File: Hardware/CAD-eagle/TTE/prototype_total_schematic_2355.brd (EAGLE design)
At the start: 39.5 x 44.9 mm, 31 parts, among them J2 MOLEX_48037-0001MOLEX_48037-0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, J4 RX

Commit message: Cascaded RX PGA array confirmed
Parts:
- added C7: 22pF, SparkFun-Capacitors:0805
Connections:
- new net ANTENNA_TX_SIG_COUPLED: C7.2, TM2.3
- net ANTENNA_TX_SIG: now also C7.1; no longer TM2.3
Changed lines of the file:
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@@
 <attribute name="PROD_ID" value="CONN-09696" x="23.114" y="24.384" size="1.778" layer="27" display="off"/>
+</element>
+<element name="C7" library="SparkFun-Capacitors" package="0805" value="22pF" x="11.43" y="-16.764">
+<attribute name="PROD_ID" value="CAP-08402" x="11.43" y="-16.764" size="1.778" layer="27" display="off"/>
 </element>
 </elements>
@@
 <signal name="ANTENNA_TX_SIG">
 <contactref element="MSP430" pad="34"/>
-<contactref element="TM2" pad="3"/>
 <contactref element="SIG" pad="2"/>
 <wire x1="25.7556" y1="35.9664" x2="21.1836" y2="31.3944" width="0.508" layer="1"/>
@@
 <wire x1="32.004" y1="39.624" x2="30.3276" y2="39.624" width="0.1524" layer="16"/>
 <wire x1="33.274" y1="38.354" x2="32.004" y2="39.624" width="0.1524" layer="16"/>
-<wire x1="21.1836" y1="31.3944" x2="21.035" y2="31.258" width="0.1524" layer="1"/>
 <wire x1="42.3672" y1="30.0228" x2="43.2816" y2="30.0228" width="0.1524" layer="1"/>
 <wire x1="41.148" y1="31.242" x2="42.3672" y2="30.0228" width="0.1524" layer="1"/>
@@
 <via x="25.7556" y="35.9664" extent="1-16" drill="0.35"/>
 <via x="41.148" y="31.242" extent="1-16" drill="0.35"/>
+<contactref element="C7" pad="1"/>
+<wire x1="10.53" y1="-16.764" x2="21.1836" y2="31.3944" width="0" layer="19" extent="1-1"/>
 </signal>
 <signal name="RX_PGA_1">
@@
 <via x="41.6052" y="10.0584" extent="1-16" drill="0.35"/>
 </signal>
+<signal name="ANTENNA_TX_SIG_COUPLED">
+<contactref element="TM2" pad="3"/>
+<contactref element="C7" pad="2"/>
+<wire x1="12.33" y1="-16.764" x2="21.035" y2="31.258" width="0" layer="19" extent="1-1"/>
+</signal>
 </signals>

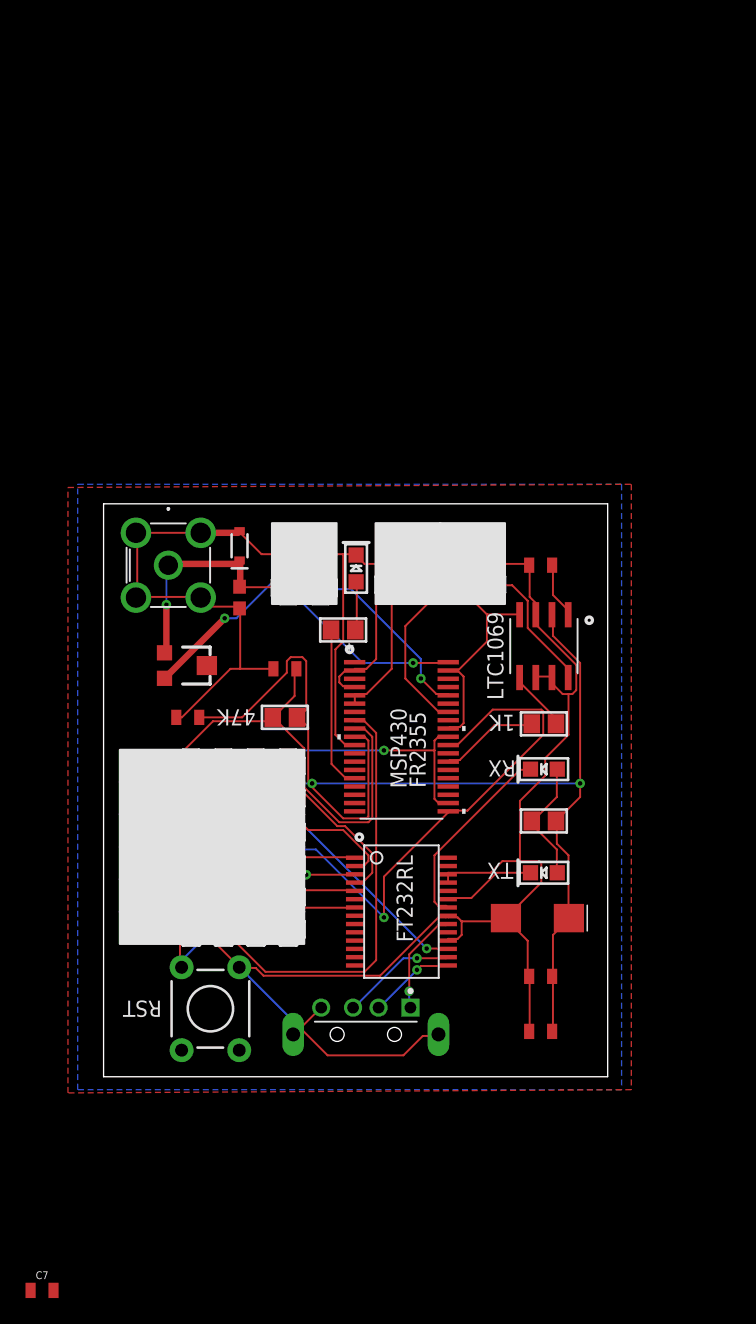
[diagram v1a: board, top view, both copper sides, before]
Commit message: Reciever Pipeline Confirmed, Updated Gerbers, included tx coupling capacitor for rx offset
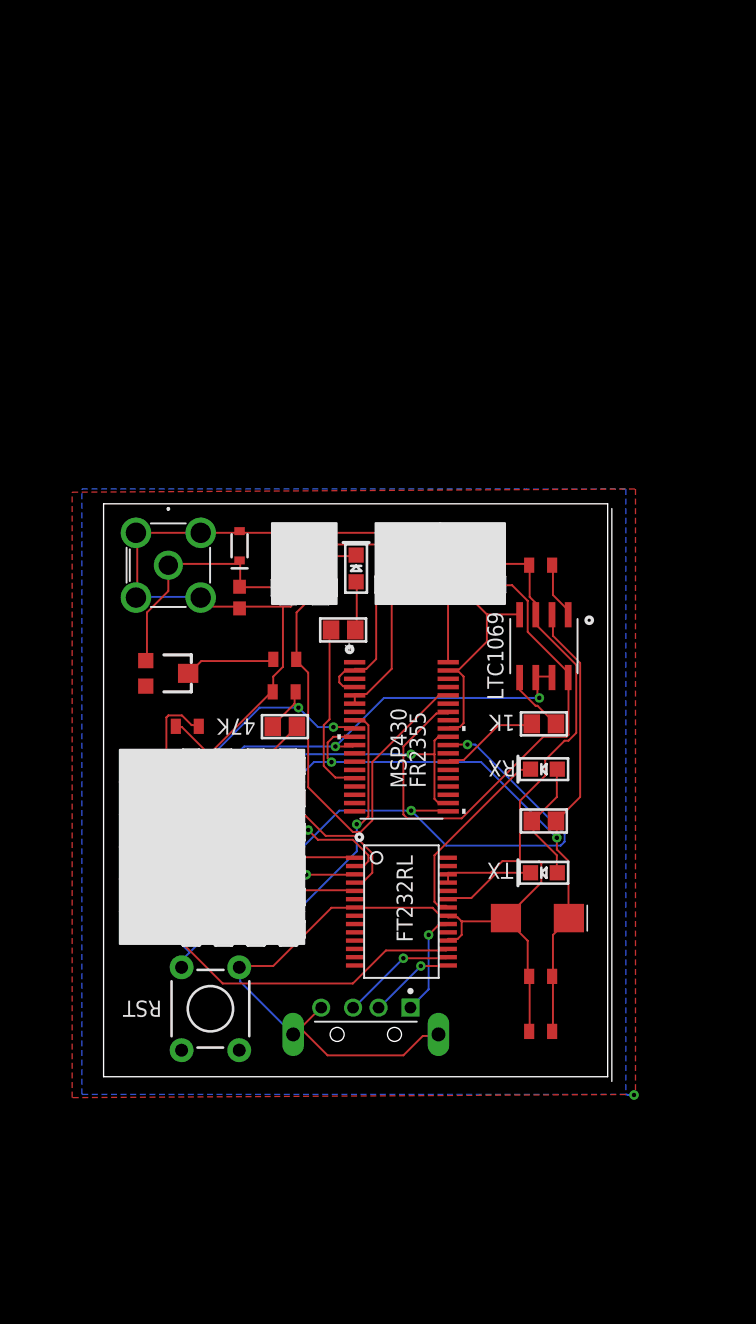
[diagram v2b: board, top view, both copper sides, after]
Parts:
- C5: value 100n -> .1u
- C7: value 22pF -> 22p
- moved C7 53.0 mm to (30.5, 32.7), turned to 180 degrees
- moved C6 1.81 mm to (30.4, 30.2)
- moved TM2 1.59 mm to (21.4, 31.6)
- moved 47K 0.73 mm to (30.5, 27.5)
- moved C5 0.70 mm to (22.8, 27.5)
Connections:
- removed net ANTENNA_TX_SIG_COUPLED: C7.2, TM2.3
- new net N$2: C7.2, TM2.2
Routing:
- net RST/SBWTDIO: track 58.7 -> 41.8 mm, vias 0 -> 2
- net FILTER_OUT: track 29.0 -> 41.3 mm
- net VCC_USB: track 45.3 -> 54.3 mm, vias 1 -> 0
- net TEST/SSBWTCK: track 33.7 -> 24.7 mm, vias 0 -> 1
- net VCC: track 98.4 -> 90.7 mm
- net ANTENNA_SIG: track 34.0 -> 41.4 mm, vias 2 -> 0
- net N$2: track 0.00 -> 7.20 mm
- net ANTENNA_TX_SIG: track 30.5 -> 36.4 mm, vias 2 -> 0
- net GND: track 212.2 -> 207.5 mm, vias 0 -> 2
- net BCLUART_RXD: track 34.8 -> 30.5 mm
- net RST/SBWTDIO_USB: track 24.4 -> 21.0 mm, vias 0 -> 1
- net STATUS_LED: track 12.8 -> 13.8 mm
- net GND1: track 0.00 -> 0.78 mm, vias 0 -> 1
- net BCLUART_TXD: track 46.1 -> 45.4 mm, vias 1 -> 2
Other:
- board size 39.5 x 44.9 mm -> 39.9 x 45.3 mm
- board text added: "Rory Hancock - Blake Stadnyk Brody Dunlop - David Lutzer"
- board text removed: "Rory Hancock | Blake Stadnyk Brody Dunlop | David Lutzer"

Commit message: MODEM Files
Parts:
- removed FILT: FILT, SparkFun-Connectors:1X02
- removed GND, RXD, TCK, TDIO, TXD, VCC: 455-1750-1-ND, SparkFun-Connectors:1X04
- removed J4, SIG: RX, SparkFun-Connectors:1X02
- removed MSP430: MSP430FR2355, TTE:DA38
- removed RIGHT_ANGLE_SMA_MALE: 5-1814400-1, TTE:5-1814400-1
- removed RST: (no value), SparkFun-Switches:TACTILE_SWITCH_PTH_6.0MM
- added J: 0, SparkFun-Resistors:0603
- added J1: (no value), SparkFun-Connectors:1X07_NO_SILK
- added MSP430FR2355: MSP430FR2355, TTE:DA38
- added RESET: (no value), SparkFun-Switches:TACTILE_SWITCH_PTH_6.0MM
- added U$1: USB-PCB, TTE:PCB_USB
- added _: (no value), TTE:5-1814400-1
- C2: value 100nF -> 22p
- C7: value 22p -> 100nF
- moved C2 70.2 mm to (46.7, 78.0), turned to 90 degrees
- moved C3 67.5 mm to (59.4, 70.5), turned to 0 degrees
- moved C5 54.4 mm to (53.7, 72.3), turned to 270 degrees
- moved C1 50.0 mm to (43.3, 62.0), turned to 90 degrees
- moved TM2 44.2 mm to (44.7, 69.2)
- moved TL069 43.3 mm to (59.6, 76.2), turned to 90 degrees
- moved D1 43.1 mm to (50.3, 77.9)
- moved R4 40.9 mm to (46.7, 73.4), turned to 90 degrees
- moved 1K 38.2 mm to (60.3, 64.6), turned to 90 degrees
- moved C4 37.7 mm to (53.8, 77.7), turned to 270 degrees
- moved TX 36.9 mm to (59.3, 51.9)
- moved J2 36.7 mm to (54.7, 26.9)
- moved FT232RL 35.1 mm to (49.1, 46.7)
- moved C7 31.3 mm to (59.2, 45.1), turned to 270 degrees
- moved RX 26.1 mm to (59.3, 48.8)
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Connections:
- removed net ADC: J4.2, MSP430.5, MSP430.6
- removed net BCLUART_RXD_EXT: RXD.3, RXD.4
- removed net BCLUART_RXD_USB: FT232RL.1, RXD.1
- removed net BCLUART_TXD_EXT: TXD.3, TXD.4
- removed net BCLUART_TXD_USB: FT232RL.5, TXD.1
- removed net GND_EXT: GND.3, GND.4
- removed net GND_USB: GND.1
- removed net RST/SBWTDIO_EXT: TDIO.3, TDIO.4
- removed net RST/SBWTDIO_USB: FT232RL.2, TDIO.1
- removed net RX_PGA_1: J4.1, MSP430.2, MSP430.4
- removed net TEST/SSBWTCK_USB: FT232RL.3, TCK.1
- removed net TST/SBWTCK_EXT: TCK.3, TCK.4
- removed net VCC_EXT: VCC.3, VCC.4
- removed net VCC_USB: FT232RL.17, FT232RL.4, VCC.1
- new net NC_5V: J1.6
- new net P1.3/UCB0SOMI/UCB0SCL/OA0+/A3: MSP430FR2355.4
- new net RX: FT232RL.1, MSP430FR2355.29
- new net RX_PGA_2: MSP430FR2355.37, MSP430FR2355.6
- new net TX: FT232RL.5, MSP430FR2355.28
- net ANTENNA_SIG: now also J.2, MSP430FR2355.38, TM2.3, _.1; no longer MSP430.38, RIGHT_ANGLE_SMA_MALE.1, SIG.1, TM2.1
- net ANTENNA_TX_SIG: now also J.1, MSP430FR2355.34, TM2.2; no longer C7.1, MSP430.34, SIG.2
- net BCLUART_RXD: now also J1.4, MSP430FR2355.21; no longer MSP430.21, MSP430.29, RXD.2
- net BCLUART_TXD: now also J1.3, MSP430FR2355.20; no longer MSP430.20, MSP430.28, TXD.2
- net FILTER_CLK: now also MSP430FR2355.26; no longer MSP430.26
- net FILTER_IN: now also MSP430FR2355.30, MSP430FR2355.36; no longer FILT.2, MSP430.30, MSP430.37
- net FILTER_OUT: now also MSP430FR2355.32; no longer FILT.1, MSP430.32
- net GND: now also C2.1, C7.2, J1.7, MSP430FR2355.11, RESET.1, U$1.P$4; no longer C2.2, GND.2, MSP430.11, RIGHT_ANGLE_SMA_MALE.2, RIGHT_ANGLE_SMA_MALE.3, RIGHT_ANGLE_SMA_MALE.4, RIGHT_ANGLE_SMA_MALE.5, RST.1
- net N$2: now also C2.2, _.2, _.3, _.4, _.5; no longer C7.2, TM2.2
- net P3.0/MCLK: now also MSP430FR2355.3; no longer MSP430.3
- net P3.6/OA3-: now also MSP430FR2355.33; no longer MSP430.33
- net RST/SBWTDIO: now also J1.2, MSP430FR2355.9, RESET.3; no longer MSP430.9, RST.3, TDIO.2
- net STATUS_LED: now also MSP430FR2355.16; no longer MSP430.15
- net TEST/SSBWTCK: now also J1.1, MSP430FR2355.8; no longer MSP430.8, TCK.2
- net USB_DATA_+: now also J2.3, U$1.P$3; no longer J2.2
- net USB_DATA_-: now also J2.2, U$1.P$2; no longer J2.3
- net VCC: now also FT232RL.17, FT232RL.4, J1.5, MSP430FR2355.10; no longer C2.1, MSP430.10, VCC.2
- net V_USB: now also C7.1, U$1.P$1
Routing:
- net VCC_USB: track 54.3 -> 0.00 mm
- net BCLUART_TXD: track 45.4 -> 22.1 mm, vias 2 -> 1
- net V_USB: track 8.16 -> 29.4 mm
- net RST/SBWTDIO_USB: track 21.0 -> 0.00 mm, vias 1 -> 0
- net FILTER_OUT: track 41.3 -> 21.7 mm, vias 0 -> 2
- net ANTENNA_TX_SIG: track 36.4 -> 18.3 mm, vias 0 -> 2
- net TX: track 0.00 -> 16.7 mm
- net RX_PGA_1: track 16.2 -> 0.00 mm
- net TEST/SSBWTCK_USB: track 15.6 -> 0.00 mm, vias 1 -> 0
- net RX: track 0.00 -> 15.1 mm
- net BCLUART_RXD_USB: track 13.7 -> 0.00 mm
- net BCLUART_TXD_USB: track 13.7 -> 0.00 mm
- net GND: track 207.5 -> 194.2 mm, vias 2 -> 1
- net USB_DATA_+: track 6.80 -> 19.5 mm
- net USB_DATA_-: track 9.06 -> 21.6 mm
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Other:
- board size 39.9 x 45.3 mm -> 28.7 x 63.8 mm
- board text added: "Blake Stadnyk Brody Dunlop Rory Hancock David Lutzer"
- board text added: "GND"
- board text added: "Rev. 2"
- board text added: "TTE-Communications ECE Capstone 2019"
- board text removed: "FR2355"
- board text removed: "I"
- board text removed: "LTC1069"
- board text removed: "O"
- board text removed: "Rory Hancock - Blake Stadnyk Brody Dunlop - David Lutzer"
- board text removed: "SIG"
- board text removed: "TTE-Boys ECE Capstone 2019"

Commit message: V3 PCB schematics Ordered
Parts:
- removed J: 0, SparkFun-Resistors:0603
- removed MSP430FR2355: MSP430FR2355, TTE:DA38
- added FILTER: (no value), microbuilder:1X02_ROUND
- added MSPFR2355-DBT: MSPFR2355-DBT, TTE:SOP50P640X120-38N
- C1: value 10µF -> 10u
- C3: value 22uF -> 22u
- C7: value 100nF -> 100n
- moved 1K 2.74 mm to (59.7, 67.3), turned to 0 degrees
- moved C1 1.69 mm to (45.0, 61.6)
- moved R2 1.37 mm to (44.5, 54.4), turned to 0 degrees
- moved R6 1.28 mm to (59.2, 42.9)
- moved C6 1.02 mm to (39.6, 43.6)
- moved C7 0.76 mm to (59.2, 45.8), turned to 0 degrees
- moved STATUS 0.65 mm to (39.8, 46.6), turned to 270 degrees
- moved D1 0.64 mm to (50.3, 77.2)
- moved TM2 0.40 mm to (44.8, 68.8)
- moved C2 0.38 mm to (47.1, 78.0)
- moved _ 0.36 mm to (40.8, 76.1), turned to 0 degrees
- moved 47K 0.28 mm to (39.8, 50.0)
- moved R4 0.25 mm to (47.0, 73.4)
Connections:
- net ANTENNA_SIG: now also MSPFR2355-DBT.38; no longer J.2, MSP430FR2355.38
- net ANTENNA_TX_SIG: now also MSPFR2355-DBT.34; no longer J.1, MSP430FR2355.34
- net BCLUART_RXD: now also MSPFR2355-DBT.21; no longer MSP430FR2355.21
- net BCLUART_TXD: now also MSPFR2355-DBT.20; no longer MSP430FR2355.20
- net FILTER_CLK: now also MSPFR2355-DBT.26; no longer MSP430FR2355.26
- net FILTER_IN: now also FILTER.2, MSPFR2355-DBT.30; no longer MSP430FR2355.30, MSP430FR2355.36
- net FILTER_OUT: now also FILTER.1, MSPFR2355-DBT.32, MSPFR2355-DBT.36; no longer MSP430FR2355.32
- net GND: now also MSPFR2355-DBT.11; no longer J2.5, J2.6, MSP430FR2355.11
- net P1.3/UCB0SOMI/UCB0SCL/OA0+/A3: now also MSPFR2355-DBT.4; no longer MSP430FR2355.4
- net P3.0/MCLK: now also MSPFR2355-DBT.3; no longer MSP430FR2355.3
- net P3.6/OA3-: now also MSPFR2355-DBT.33; no longer MSP430FR2355.33
- net RST/SBWTDIO: now also MSPFR2355-DBT.9; no longer MSP430FR2355.9
- net RX: now also MSPFR2355-DBT.29; no longer MSP430FR2355.29
- net RX_PGA_2: now also MSPFR2355-DBT.37, MSPFR2355-DBT.6; no longer MSP430FR2355.37, MSP430FR2355.6
- net STATUS_LED: now also MSPFR2355-DBT.16; no longer MSP430FR2355.16
- net TEST/SSBWTCK: now also MSPFR2355-DBT.8; no longer MSP430FR2355.8
- net TX: now also MSPFR2355-DBT.28; no longer MSP430FR2355.28
- net VCC: now also MSPFR2355-DBT.10; no longer MSP430FR2355.10
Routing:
- net GND: track 194.2 -> 142.0 mm, vias 1 -> 0
- net N$19: track 7.88 -> 34.2 mm
- net TEST/SSBWTCK: track 30.7 -> 18.7 mm
- net N$20: track 6.15 -> 17.9 mm
- net VCC: track 93.3 -> 86.3 mm, vias 4 -> 2
- net TX: track 16.7 -> 22.0 mm, vias 0 -> 2
- net FILTER_OUT: track 21.7 -> 26.8 mm, vias 2 -> 0
- net FILTER_CLK: track 7.32 -> 11.7 mm, vias 0 -> 2
- net RST/SBWTDIO: track 40.5 -> 44.7 mm, vias 0 -> 1
- net N$21: track 7.25 -> 11.1 mm
- net ANTENNA_SIG: track 37.7 -> 41.4 mm, vias 2 -> 1
- net ANTENNA_TX_SIG: track 18.3 -> 15.0 mm
- net BCLUART_TXD: track 22.1 -> 18.8 mm
- net V_USB: track 29.4 -> 32.4 mm, vias 1 -> 2
- net FILTER_IN: track 17.0 -> 19.0 mm, vias 0 -> 1
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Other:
- outline, holes or cut-outs redrawn
- board text added: "3V3"
- board text added: "In"
- board text added: "NC"
- board text added: "Out"
- board text added: "RX"
- board text added: "SBWIO-CK"
- board text added: "TX"
- board text added: "V3"
- board text removed: "Rev. 2"
